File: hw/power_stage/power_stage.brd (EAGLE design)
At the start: 100 x 100 mm, 54 parts, among them IC1H MIC4420M, IC1L MIC4429M, IC2H MIC4420M, IC2L MIC4429M

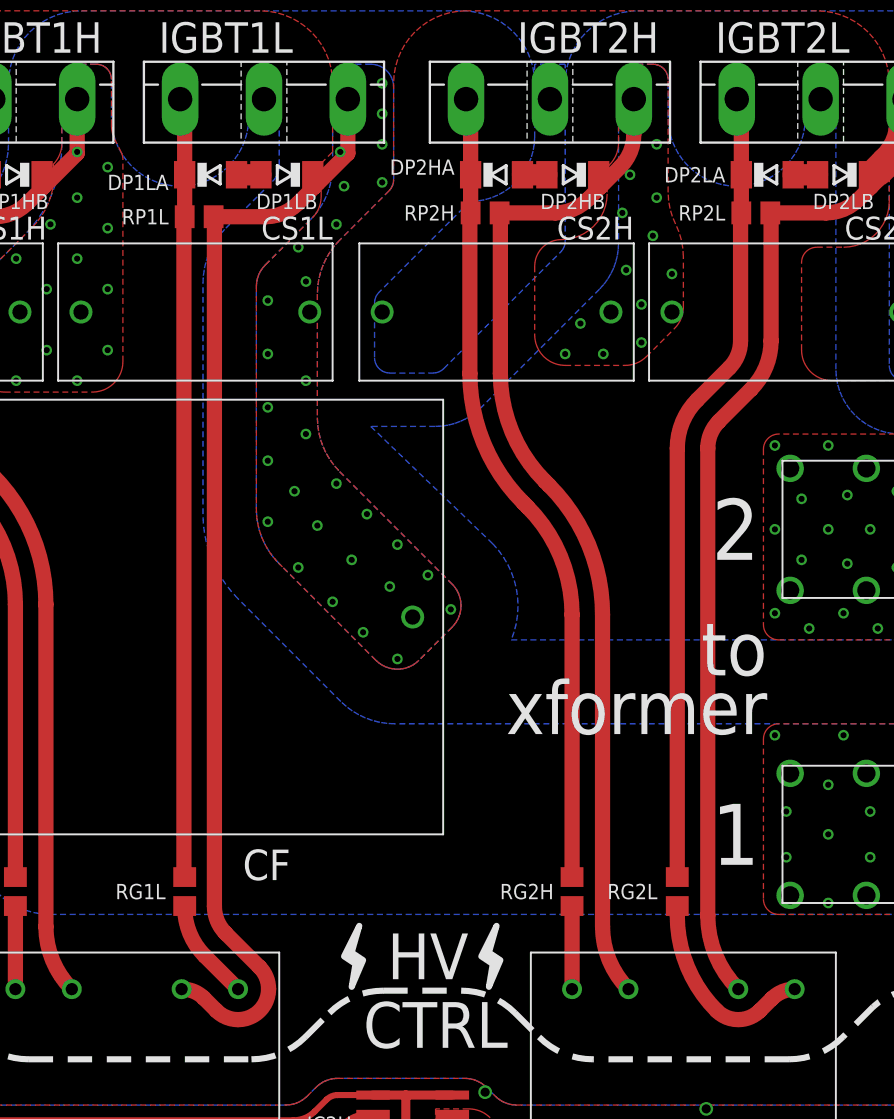
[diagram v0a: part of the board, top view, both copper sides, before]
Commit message: Power stage: fix incorrect GDT footprint
Turns out I must've measured wrong when i determined the polarity of the
GDT windings, but one of the secondary windings has the opposite
polarity to what I had in the layout. Makes sense, since this does make
the layout somewhat more direct.

Doesn't matter much now since my boards have already been produced (I'll
be patching them by hand) and it's unlikely anyone will end up using the
same GDTs, but just in case, I figured I'd make it easier on myself when
referring to the design files.
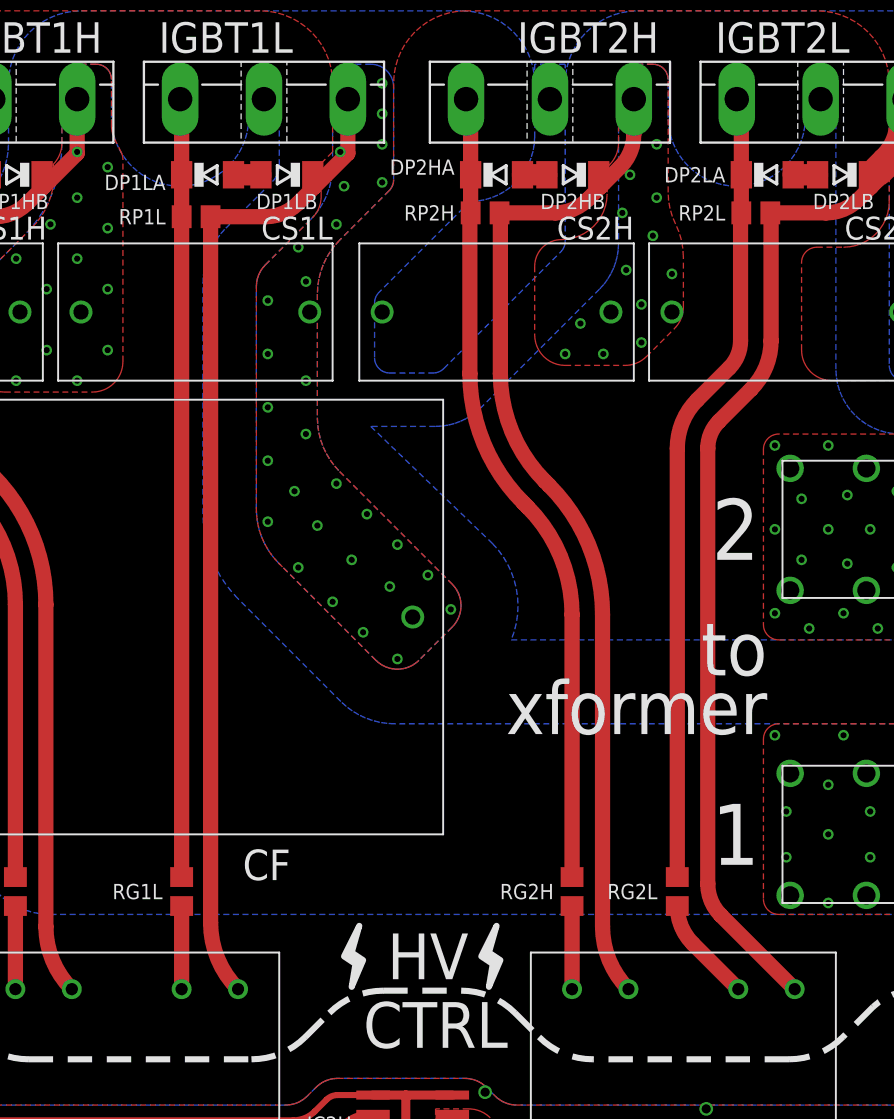
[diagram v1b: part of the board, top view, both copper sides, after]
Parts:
- moved DP1LA 0.20 mm to (50.8, 76.0)
- moved RP1L 0.20 mm to (50.0, 73.2)
- moved RG1L 0.20 mm to (49.1, 29.0)
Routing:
- net N$12: track 12.9 -> 6.89 mm
- net V-: track 140.7 -> 134.7 mm
- net N$7: track 6.62 -> 5.45 mm
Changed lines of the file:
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@@
 <setting verticaltext="up"/>
 </settings>
-<grid distance="1" unitdist="mm" unit="mm" style="lines" multiple="1" display="no" altdistance="0.25" altunitdist="mm" altunit="mm"/>
+<grid distance="1" unitdist="mm" unit="mm" style="lines" multiple="1" display="no" altdistance="0.1" altunitdist="mm" altunit="mm"/>
 <layers>
 <layer number="1" name="Top" color="4" fill="1" visible="yes" active="yes"/>
@@
 <layer number="45" name="Holes" color="7" fill="1" visible="yes" active="yes"/>
 <layer number="46" name="Milling" color="3" fill="1" visible="yes" active="yes"/>
-<layer number="47" name="Measures" color="7" fill="1" visible="no" active="yes"/>
+<layer number="47" name="Measures" color="7" fill="1" visible="yes" active="yes"/>
 <layer number="48" name="Document" color="7" fill="1" visible="yes" active="yes"/>
 <layer number="49" name="Reference" color="7" fill="1" visible="yes" active="yes"/>
@@
 <text x="87" y="52.75" size="4" layer="21" font="vector" ratio="15" align="center-right">2</text>
 <text x="87" y="32.75" size="4" layer="21" font="vector" ratio="15" align="center-right">1</text>
+<wire x1="115" y1="60.25" x2="115" y2="45.25" width="0.4064" layer="47"/>
+<wire x1="-4" y1="84" x2="-1.75" y2="84" width="0.4064" layer="47"/>
 </plain>
 <attributes>
@@
 <attribute name="VALUE" x="40.74" y="28.365" size="1.27" layer="27" rot="R90"/>
 </element>
-<element name="RG1L" library="rcl" package="R0805" value="" x="49.3" y="29" smashed="yes" rot="R90">
-<attribute name="NAME" x="48.05" y="29" size="1" layer="25" font="vector" ratio="15" align="center-right"/>
-<attribute name="VALUE" x="51.84" y="28.365" size="1.27" layer="27" rot="R90"/>
+<element name="RG1L" library="rcl" package="R0805" value="" x="49.1" y="29" smashed="yes" rot="R90">
+<attribute name="NAME" x="47.85" y="29" size="1" layer="25" font="vector" ratio="15" align="center-right"/>
+<attribute name="VALUE" x="51.64" y="28.365" size="1.27" layer="27" rot="R90"/>
 </element>
 <element name="RG2L" library="rcl" package="R0805" value="" x="81.6" y="29" smashed="yes" rot="R90">
@@
 <attribute name="VALUE" x="33.135" y="75.79" size="1.27" layer="27" rot="R180"/>
 </element>
-<element name="RP1L" library="rcl" package="R0805" value="" x="50.25" y="73.25" smashed="yes" rot="R180">
-<attribute name="NAME" x="48.25" y="73.25" size="1" layer="25" font="vector" ratio="15" align="center-right"/>
-<attribute name="VALUE" x="50.885" y="75.79" size="1.27" layer="27" rot="R180"/>
+<element name="RP1L" library="rcl" package="R0805" value="" x="50.05" y="73.25" smashed="yes" rot="R180">
+<attribute name="NAME" x="48.05" y="73.25" size="1" layer="25" font="vector" ratio="15" align="center-right"/>
+<attribute name="VALUE" x="50.685" y="75.79" size="1.27" layer="27" rot="R180"/>
 </element>
 <element name="RP2L" library="rcl" package="R0805" value="" x="86.75" y="73.5" smashed="yes" rot="R180">
@@
 <attribute name="VALUE" x="39.774" y="78.413" size="1.27" layer="27" rot="R180"/>
 </element>
-<element name="DP1LA" library="diode" package="SOD80C" value="" x="51" y="76" smashed="yes">
-<attribute name="NAME" x="48.25" y="75.5" size="1" layer="25" font="vector" ratio="15" align="center-right"/>
-<attribute name="VALUE" x="49.476" y="73.587" size="1.27" layer="27"/>
+<element name="DP1LA" library="diode" package="SOD80C" value="" x="50.8" y="76" smashed="yes">
+<attribute name="NAME" x="48.05" y="75.5" size="1" layer="25" font="vector" ratio="15" align="center-right"/>
+<attribute name="VALUE" x="49.276" y="73.587" size="1.27" layer="27"/>
 </element>
 <element name="DP1LB" library="diode" package="SOD80C" value="" x="56" y="76" smashed="yes" rot="R180">
@@
 <contactref element="RP1L" pad="2"/>
 <contactref element="DP1LA" pad="C"/>
-<wire x1="49.3" y1="73.25" x2="49.3" y2="76" width="1" layer="1"/>
-<wire x1="49" y1="80.96" x2="49.3" y2="80.66" width="1" layer="1"/>
-<wire x1="49.3" y1="80.66" x2="49.3" y2="76" width="1" layer="1"/>
 <contactref element="RG1L" pad="2"/>
-<wire x1="49.3" y1="29.95" x2="49.25" y2="29.95" width="1" layer="1"/>
-<wire x1="49.25" y1="29.95" x2="49.25" y2="73.25" width="1" layer="1"/>
-<wire x1="49.25" y1="73.25" x2="49.3" y2="73.25" width="1" layer="1"/>
+<wire x1="49.1" y1="73.25" x2="49.1" y2="29.95" width="1" layer="1"/>
+<wire x1="49.1" y1="76" x2="49.1" y2="73.25" width="1" layer="1"/>
+<wire x1="49" y1="80.96" x2="49.1" y2="80.86" width="1" layer="1"/>
+<wire x1="49.1" y1="80.86" x2="49.1" y2="76" width="1" layer="1"/>
 </signal>
 <signal name="N$7" class="1">
 <contactref element="RG1L" pad="1"/>
 <contactref element="GDT1" pad="S2B"/>
-<wire x1="52.8" y1="22.6" x2="50.61801875" y2="24.78198125" width="1" layer="1"/>
-<wire x1="50.61801875" y1="24.78198125" x2="49.3" y2="27.9639625" width="1" layer="1" curve="-45"/>
-<wire x1="49.3" y1="27.9639625" x2="49.3" y2="28.05" width="1" layer="1"/>
+<wire x1="49.1" y1="28.05" x2="49.1" y2="22.6" width="1" layer="1"/>
 </signal>
 <signal name="N$10" class="1">
@@
 <contactref element="RG2L" pad="1"/>
 <contactref element="GDT2" pad="S2B"/>
-<wire x1="81.6" y1="28.05" x2="81.6" y2="27.42843125" width="1" layer="1"/>
-<wire x1="81.6" y1="27.42843125" x2="84.1857875" y2="21.1857875" width="1" layer="1" curve="45"/>
-<wire x1="84.1857875" y1="21.1857875" x2="87.0142125" y2="21.1857875" width="1" layer="1" curve="90"/>
-<wire x1="87.0142125" y1="21.1857875" x2="87.812128125" y2="21.983703125" width="1" layer="1"/>
-<wire x1="87.812128125" y1="21.983703125" x2="89.3" y2="22.6" width="1" layer="1" curve="-45"/>
+<wire x1="85.6" y1="22.6" x2="82.62530625" y2="25.57469375" width="1" layer="1"/>
+<wire x1="82.62530625" y1="25.57469375" x2="81.6" y2="28.05" width="1" layer="1" curve="-45"/>
 </signal>
 <signal name="N$13" class="1">
@@
 <contactref element="DP1LA" pad="A"/>
 <contactref element="DP1LB" pad="A"/>
-<wire x1="52.7" y1="76" x2="54.3" y2="76" width="1.4" layer="1"/>
+<wire x1="52.5" y1="76" x2="54.3" y2="76" width="1.4" layer="1"/>
 </signal>
 <signal name="N$23">
@@
 <vertex x="23.5" y="78.25" curve="-90"/>
 </polygon>
-<wire x1="51.2" y1="73.25" x2="54.607359375" y2="73.25" width="1" layer="1"/>
+<wire x1="51" y1="73.25" x2="54.607359375" y2="73.25" width="1" layer="1"/>
 <wire x1="54.607359375" y1="73.25" x2="56.728678125" y2="74.128678125" width="1" layer="1" curve="44.999958"/>
 <wire x1="56.728678125" y1="74.128678125" x2="57.8" y2="75.2" width="1" layer="1"/>
@@
 <wire x1="94.75" y1="76.25" x2="94.75" y2="75.65" width="1" layer="1"/>
 <wire x1="94.75" y1="75.65" x2="94.3" y2="75.2" width="1" layer="1"/>
-<wire x1="51.2" y1="73.25" x2="51.25" y2="73.25" width="1" layer="1"/>
-<wire x1="51.25" y1="73.25" x2="51.25" y2="28.035534375" width="1" layer="1"/>
-<wire x1="51.25" y1="28.035534375" x2="51.982234375" y2="26.267765625" width="1" layer="1" curve="45.000051"/>
-<wire x1="51.982234375" y1="26.267765625" x2="54.2142125" y2="24.0357875" width="1" layer="1"/>
-<wire x1="54.2142125" y1="24.0357875" x2="54.8" y2="22.621571875" width="1" layer="1" curve="-45.00009"/>
-<wire x1="54.8" y1="22.621571875" x2="54.8" y2="22.6" width="1" layer="1"/>
-<wire x1="54.8" y1="22.6" x2="52.8" y2="20.6" width="1" layer="1" curve="-90"/>
-<wire x1="52.8" y1="20.6" x2="51.385790625" y2="21.185784375" width="1" layer="1" curve="-45"/>
-<wire x1="51.385790625" y1="21.185784375" x2="50.5573625" y2="22.0142125" width="1" layer="1"/>
-<wire x1="50.5573625" y1="22.0142125" x2="49.143146875" y2="22.6" width="1" layer="1" curve="45.00009"/>
-<wire x1="49.143146875" y1="22.6" x2="49.1" y2="22.6" width="1" layer="1"/>
 <wire x1="83.6" y1="58.064465625" x2="84.332234375" y2="59.832234375" width="1" layer="1" curve="-45.000051"/>
 <wire x1="84.332234375" y1="59.832234375" x2="86.43198125" y2="61.93198125" width="1" layer="1"/>
@@
 <wire x1="87.75" y1="65.1139625" x2="87.75" y2="73.5" width="1" layer="1"/>
 <wire x1="87.75" y1="73.5" x2="87.7" y2="73.5" width="1" layer="1"/>
-<wire x1="83.6" y1="58.064465625" x2="83.6" y2="27.428428125" width="1" layer="1"/>
-<wire x1="83.6" y1="27.428428125" x2="85.6" y2="22.6" width="1" layer="1" curve="45"/>
+<wire x1="89.3" y1="22.6" x2="84.447821875" y2="27.452178125" width="1" layer="1"/>
+<wire x1="84.447821875" y1="27.452178125" x2="83.6" y2="29.499" width="1" layer="1" curve="-45"/>
+<wire x1="83.6" y1="29.499" x2="83.6" y2="58.064465625" width="1" layer="1"/>
 <via x="23.25" y="82" extent="1-16" drill="0.4"/>
 <via x="26" y="82" extent="1-16" drill="0.4"/>
@@
 <via x="62.25" y="75.5" extent="1-16" drill="0.4"/>
 <via x="62.25" y="80" extent="1-16" drill="0.4"/>
+<wire x1="52.8" y1="22.6" x2="51" y2="26.945584375" width="1" layer="1" curve="-45"/>
+<wire x1="51" y1="26.945584375" x2="51" y2="73.25" width="1" layer="1"/>
 </signal>
 <signal name="V+">

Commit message: Clean up the power stage schematic
This means the board changed a bit too
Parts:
- CB: device rcl:E2,5-7 -> passives:CPOL-PANASONIC-B
- CB1H, CB1L, CB2H, CB2L, CG1I, CG2I: device rcl:C0805 -> passives:C-0805
- CF: device induction-heater:R75 -> induction-heater:C-R75
- CS1H, CS1L, CS2H, CS2L: device induction-heater:R76 -> induction-heater:C-R76
- DP1HA, DP1HB, DP1LA, DP1LB, DP2HA, DP2HB, DP2LA, DP2LB: value (none) -> 20 V; device diode:SOD80C -> induction-heater:SOD80C
- RG1H, RG1L, RG2H, RG2L: value (none) -> 47 Ω; device rcl:R0805 -> passives:R-0805
- RG1I, RG2I: device rcl:R0805 -> passives:R-0805
- RP1H, RP1L, RP2H, RP2L: value (none) -> 10 kΩ; device rcl:R0805 -> passives:R-0805
- moved CB 1.00 mm to (16.0, 20.0)
- turned IC1H to 0 degrees
- turned IC1L to 0 degrees
- turned IC2H to 0 degrees
- turned IC2L to 0 degrees
- turned JP2 to 270 degrees
- renumbered BR to BR1
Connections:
- removed net VCC: CB.+, CB1H.1, CB1L.1, CB2H.1, CB2L.1, IC1H.1, IC1H.8, IC1L.1, IC1L.8, IC2H.1, IC2H.8, IC2L.1, IC2L.8, JP2.2
- new net +12V: CB.+, CB1H.1, CB1L.1, CB2H.1, CB2L.1, IC1H.1, IC1H.8, IC1L.1, IC1L.8, IC2H.1, IC2H.8, IC2L.1, IC2L.8, JP2.1
- net GND: now also JP2.2; no longer JP2.1
- net N$1: now also GDT1.PRI-2; no longer GDT1.PB
- net N$12: now also GDT2.SEC2-1; no longer GDT2.S2B
- net N$13: now also GDT2.SEC1-1; no longer GDT2.S1A
- net N$26: now also GDT1.PRI-1; no longer GDT1.PA
- net N$27: now also GDT2.PRI-1; no longer GDT2.PA
- net N$3: now also GDT1.SEC1-1; no longer GDT1.S1A
- net N$5: now also GDT2.PRI-2; no longer GDT2.PB
- net N$7: now also GDT1.SEC2-1; no longer GDT1.S2B
- net OUT1: now also GDT1.SEC1-2; no longer GDT1.S1B
- net OUT2: now also GDT2.SEC1-2; no longer GDT2.S1B
- net V-: now also GDT1.SEC2-2, GDT2.SEC2-2; no longer GDT1.S2A, GDT2.S2A
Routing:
- net +12V: track 0.00 -> 115.3 mm
- net VCC: track 115.3 -> 0.00 mm, vias 1 -> 0

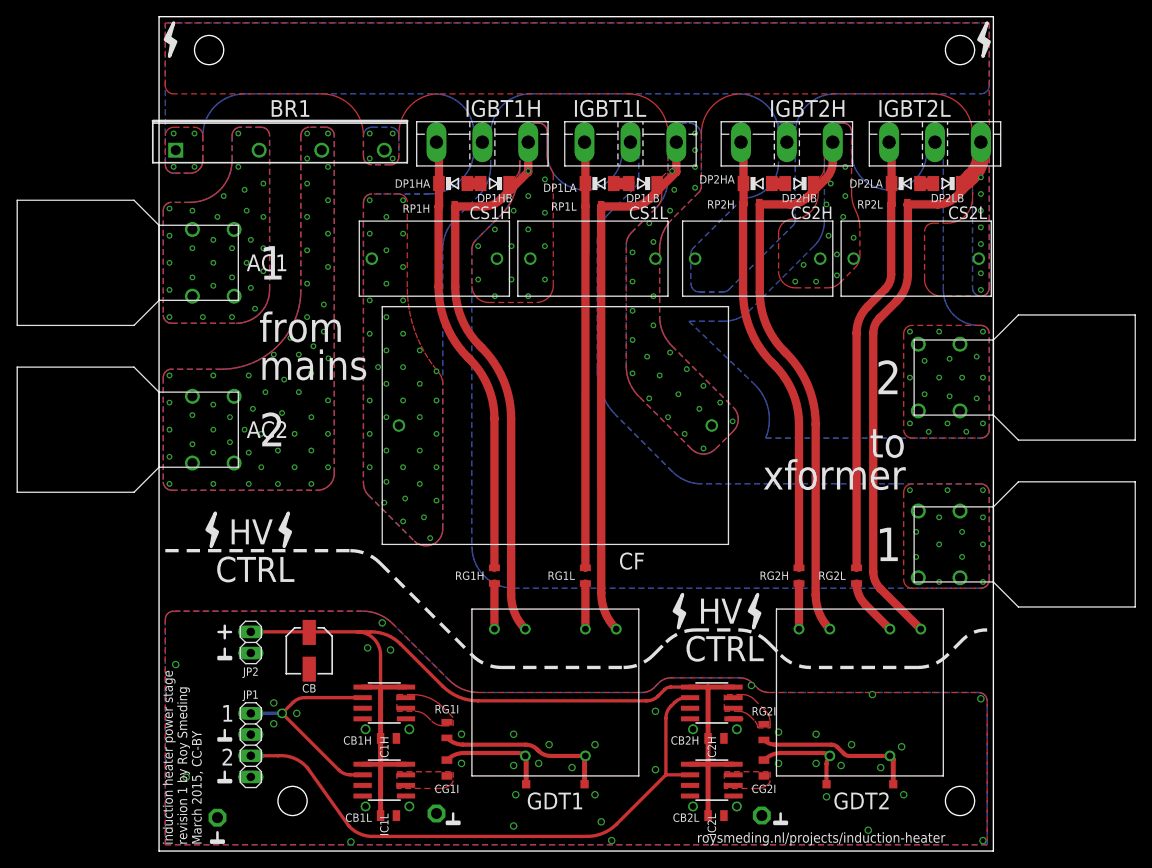
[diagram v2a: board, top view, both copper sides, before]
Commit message: Changed power stage PCB connectors
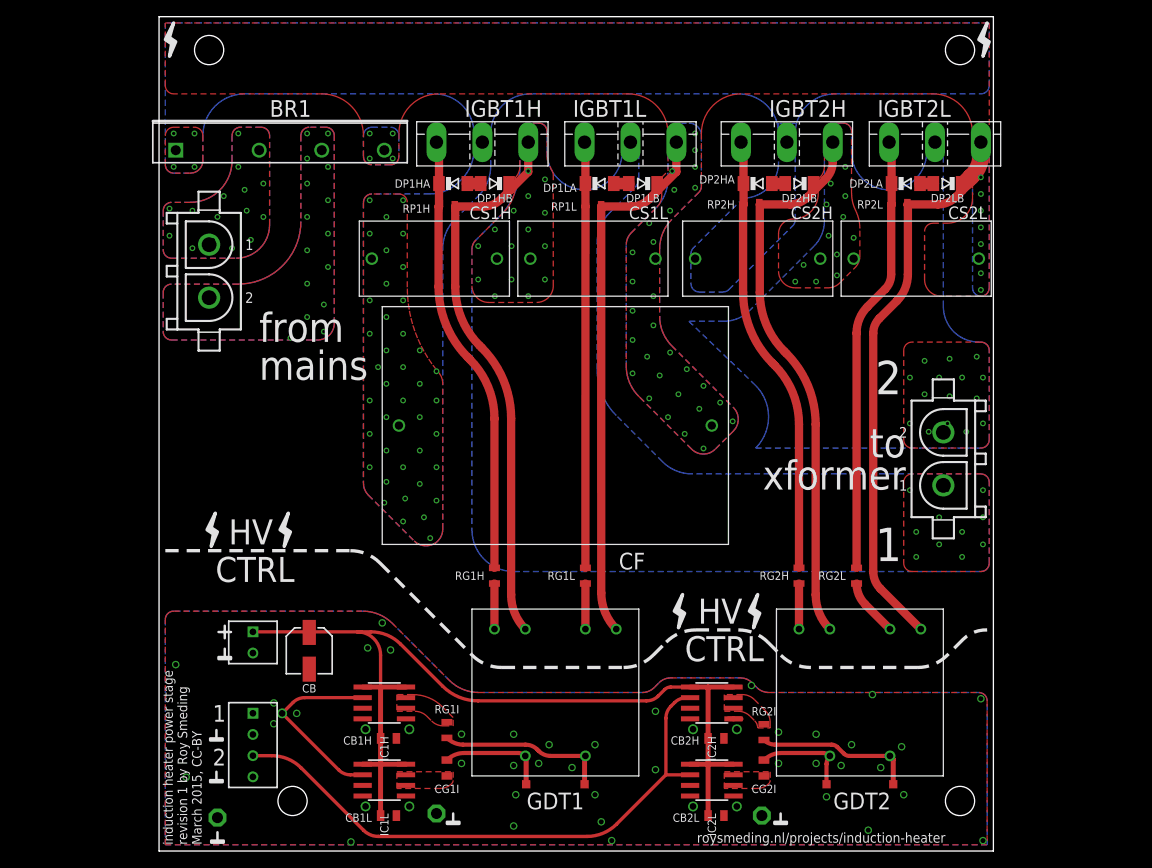
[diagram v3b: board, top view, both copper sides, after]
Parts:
- removed AC1: AC1, induction-heater:SCREW
- removed AC2: AC2, induction-heater:SCREW
- removed JP1: control, pinhead:1X04
- removed JP2: power, pinhead:1X02
- removed OUT1: OUT1, induction-heater:SCREW
- removed OUT2: OUT2, induction-heater:SCREW
- added J1: CON-2POS-NS25, induction-heater:CON-2POS-NS25
- added J2: CON-4POS-NS25, induction-heater:CON-4POS-NS25
- added J3, J4: CON-2POS-MNL, induction-heater:TE-350824-1
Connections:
- net +12V: now also J1.1; no longer JP2.1
- net AC1: now also J3.1; no longer AC1.P$1, AC1.P$2, AC1.P$3, AC1.P$4
- net AC2: now also J3.2; no longer AC2.P$1, AC2.P$2, AC2.P$3, AC2.P$4
- net GND: now also J1.2, J2.2, J2.4; no longer JP1.2, JP1.4, JP2.2
- net N$15: now also J2.1; no longer JP1.1
- net N$20: now also J2.3; no longer JP1.3
- net OUT1: now also J4.1; no longer OUT1.P$1, OUT1.P$2, OUT1.P$3, OUT1.P$4
- net OUT2: now also J4.2; no longer OUT2.P$1, OUT2.P$2, OUT2.P$3, OUT2.P$4
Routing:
- net N$15: track 26.6 -> 22.9 mm
- net N$20: track 72.0 -> 69.6 mm
- net OUT2: vias 30 -> 27
- net OUT1: vias 28 -> 26
